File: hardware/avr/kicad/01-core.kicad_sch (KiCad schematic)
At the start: 18 parts, among them U1 ATmega1284P-PU, Y1 8MHz

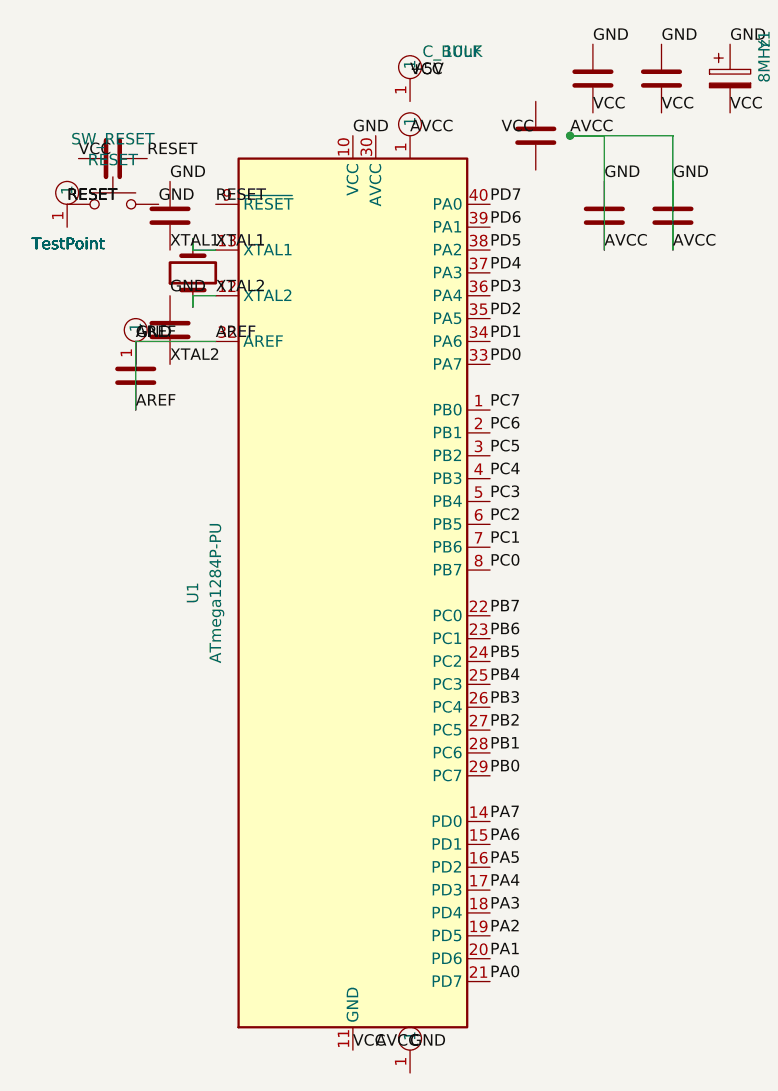
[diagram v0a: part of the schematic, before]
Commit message: Align AVR net labels with actual MCU pin endpoints
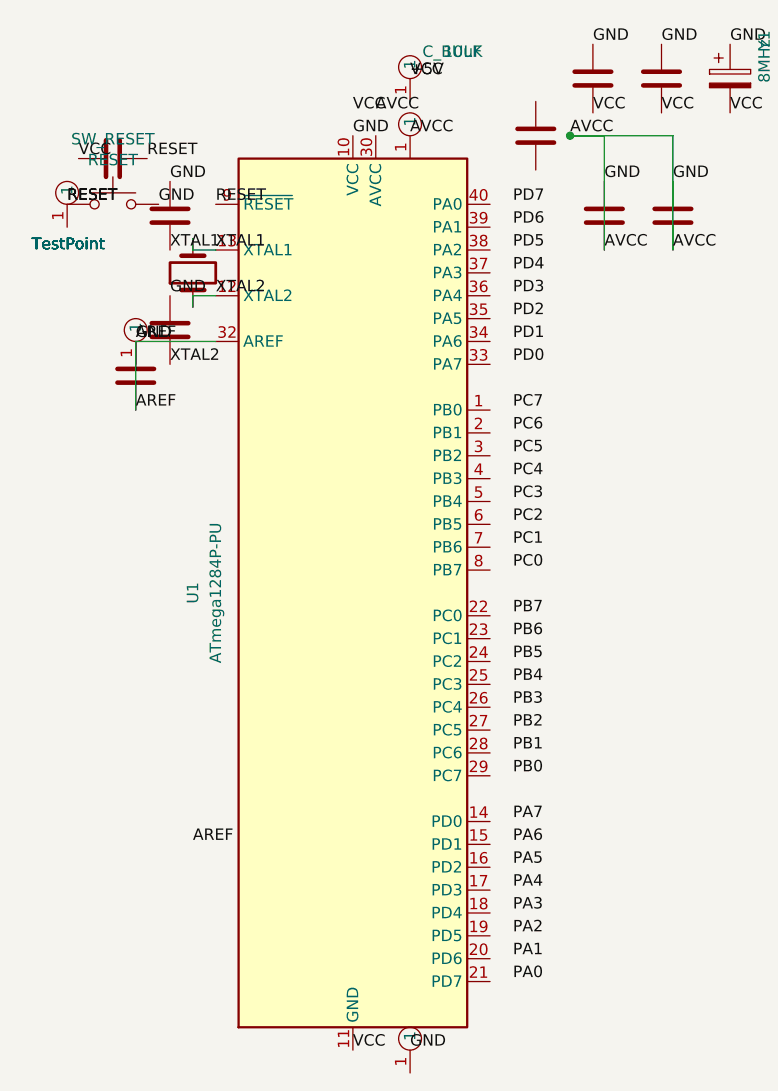
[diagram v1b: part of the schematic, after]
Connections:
- net PA0: no longer U1.21 (PD7)
- net PA1: no longer U1.20 (PD6)
- net PA2: no longer U1.19 (PD5)
- net PA3: no longer U1.18 (PD4)
- net PA4: no longer U1.17 (PD3)
- net PA5: no longer U1.16 (PD2)
- net PA6: no longer U1.15 (PD1)
- net PA7: no longer U1.14 (PD0)
- net PB0: no longer U1.29 (PC7)
- net PB1: no longer U1.28 (PC6)
- net PB2: no longer U1.27 (PC5)
- net PB3: no longer U1.26 (PC4)
- net PB4: no longer U1.25 (PC3)
- net PB5: no longer U1.24 (PC2)
- net PB6: no longer U1.23 (PC1)
- net PB7: no longer U1.22 (PC0)
- net PC0: no longer U1.8 (PB7)
- net PC1: no longer U1.7 (PB6)
- net PC2: no longer U1.6 (PB5)
- net PC3: no longer U1.5 (PB4)
- net PC4: no longer U1.4 (PB3)
- net PC5: no longer U1.3 (PB2)
- net PC6: no longer U1.2 (PB1)
- net PC7: no longer U1.1 (PB0)
- net PD0: no longer U1.33 (PA7)
- net PD1: no longer U1.34 (PA6)
- net PD2: no longer U1.35 (PA5)
- net PD3: no longer U1.36 (PA4)
- net PD4: no longer U1.37 (PA3)
- net PD5: no longer U1.38 (PA2)
- net PD6: no longer U1.39 (PA1)
- net PD7: no longer U1.40 (PA0)
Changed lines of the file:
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@@
 (kicad_sch (version 20230121) (generator eeschema)
   (paper "A4")
-  (label "PB0" (at 72.39 100.33 0) (fields_autoplaced)
+  (label "PB0" (at 74.93 100.33 0) (fields_autoplaced)
     (effects (font (size 1.27 1.27)) (justify left bottom))
   )
-  (label "PB1" (at 72.39 97.79 0) (fields_autoplaced)
+  (label "PB1" (at 74.93 97.79 0) (fields_autoplaced)
     (effects (font (size 1.27 1.27)) (justify left bottom))
   )
-  (label "PB2" (at 72.39 95.25 0) (fields_autoplaced)
+  (label "PB2" (at 74.93 95.25 0) (fields_autoplaced)
     (effects (font (size 1.27 1.27)) (justify left bottom))
   )
-  (label "PB3" (at 72.39 92.71 0) (fields_autoplaced)
+  (label "PB3" (at 74.93 92.71 0) (fields_autoplaced)
     (effects (font (size 1.27 1.27)) (justify left bottom))
   )
-  (label "PB4" (at 72.39 90.17 0) (fields_autoplaced)
+  (label "PB4" (at 74.93 90.17 0) (fields_autoplaced)
     (effects (font (size 1.27 1.27)) (justify left bottom))
   )
-  (label "PB5" (at 72.39 87.63 0) (fields_autoplaced)
+  (label "PB5" (at 74.93 87.63 0) (fields_autoplaced)
     (effects (font (size 1.27 1.27)) (justify left bottom))
   )
-  (label "PB6" (at 72.39 85.09 0) (fields_autoplaced)
+  (label "PB6" (at 74.93 85.09 0) (fields_autoplaced)
     (effects (font (size 1.27 1.27)) (justify left bottom))
   )
-  (label "PB7" (at 72.39 82.55 0) (fields_autoplaced)
+  (label "PB7" (at 74.93 82.55 0) (fields_autoplaced)
     (effects (font (size 1.27 1.27)) (justify left bottom))
   )
-  (label "PC0" (at 72.39 77.47 0) (fields_autoplaced)
+  (label "PC0" (at 74.93 77.47 0) (fields_autoplaced)
     (effects (font (size 1.27 1.27)) (justify left bottom))
   )
-  (label "PC1" (at 72.39 74.93 0) (fields_autoplaced)
+  (label "PC1" (at 74.93 74.93 0) (fields_autoplaced)
     (effects (font (size 1.27 1.27)) (justify left bottom))
   )
-  (label "PC2" (at 72.39 72.39 0) (fields_autoplaced)
+  (label "PC2" (at 74.93 72.39 0) (fields_autoplaced)
     (effects (font (size 1.27 1.27)) (justify left bottom))
   )
-  (label "PC3" (at 72.39 69.85 0) (fields_autoplaced)
+  (label "PC3" (at 74.93 69.85 0) (fields_autoplaced)
     (effects (font (size 1.27 1.27)) (justify left bottom))
   )
-  (label "PC4" (at 72.39 67.31 0) (fields_autoplaced)
+  (label "PC4" (at 74.93 67.31 0) (fields_autoplaced)
     (effects (font (size 1.27 1.27)) (justify left bottom))
   )
-  (label "PC5" (at 72.39 64.77 0) (fields_autoplaced)
+  (label "PC5" (at 74.93 64.77 0) (fields_autoplaced)
     (effects (font (size 1.27 1.27)) (justify left bottom))
   )
-  (label "PC6" (at 72.39 62.23 0) (fields_autoplaced)
+  (label "PC6" (at 74.93 62.23 0) (fields_autoplaced)
     (effects (font (size 1.27 1.27)) (justify left bottom))
   )
-  (label "PC7" (at 72.39 59.69 0) (fields_autoplaced)
+  (label "PC7" (at 74.93 59.69 0) (fields_autoplaced)
     (effects (font (size 1.27 1.27)) (justify left bottom))
   )
-  (label "PD0" (at 72.39 54.61 0) (fields_autoplaced)
+  (label "PD0" (at 74.93 54.61 0) (fields_autoplaced)
     (effects (font (size 1.27 1.27)) (justify left bottom))
   )
-  (label "PD1" (at 72.39 52.07 0) (fields_autoplaced)
+  (label "PD1" (at 74.93 52.07 0) (fields_autoplaced)
     (effects (font (size 1.27 1.27)) (justify left bottom))
   )
-  (label "PD2" (at 72.39 49.53 0) (fields_autoplaced)
+  (label "PD2" (at 74.93 49.53 0) (fields_autoplaced)
     (effects (font (size 1.27 1.27)) (justify left bottom))
   )
-  (label "PD3" (at 72.39 46.99 0) (fields_autoplaced)
+  (label "PD3" (at 74.93 46.99 0) (fields_autoplaced)
     (effects (font (size 1.27 1.27)) (justify left bottom))
   )
-  (label "PD4" (at 72.39 44.45 0) (fields_autoplaced)
+  (label "PD4" (at 74.93 44.45 0) (fields_autoplaced)
     (effects (font (size 1.27 1.27)) (justify left bottom))
   )
-  (label "PD5" (at 72.39 41.91 0) (fields_autoplaced)
+  (label "PD5" (at 74.93 41.91 0) (fields_autoplaced)
     (effects (font (size 1.27 1.27)) (justify left bottom))
   )
-  (label "PD6" (at 72.39 39.37 0) (fields_autoplaced)
+  (label "PD6" (at 74.93 39.37 0) (fields_autoplaced)
     (effects (font (size 1.27 1.27)) (justify left bottom))
   )
-  (label "PD7" (at 72.39 36.83 0) (fields_autoplaced)
+  (label "PD7" (at 74.93 36.83 0) (fields_autoplaced)
     (effects (font (size 1.27 1.27)) (justify left bottom))
   )
-  (label "PA7" (at 72.39 105.41 0) (fields_autoplaced)
+  (label "PA7" (at 74.93 105.41 0) (fields_autoplaced)
     (effects (font (size 1.27 1.27)) (justify left bottom))
   )
-  (label "PA6" (at 72.39 107.95 0) (fields_autoplaced)
+  (label "PA6" (at 74.93 107.95 0) (fields_autoplaced)
     (effects (font (size 1.27 1.27)) (justify left bottom))
   )
-  (label "PA5" (at 72.39 110.49 0) (fields_autoplaced)
+  (label "PA5" (at 74.93 110.49 0) (fields_autoplaced)
     (effects (font (size 1.27 1.27)) (justify left bottom))
   )
-  (label "PA4" (at 72.39 113.03 0) (fields_autoplaced)
+  (label "PA4" (at 74.93 113.03 0) (fields_autoplaced)
     (effects (font (size 1.27 1.27)) (justify left bottom))
   )
-  (label "PA3" (at 72.39 115.57 0) (fields_autoplaced)
+  (label "PA3" (at 74.93 115.57 0) (fields_autoplaced)
     (effects (font (size 1.27 1.27)) (justify left bottom))
   )
-  (label "PA2" (at 72.39 118.11 0) (fields_autoplaced)
+  (label "PA2" (at 74.93 118.11 0) (fields_autoplaced)
     (effects (font (size 1.27 1.27)) (justify left bottom))
   )
-  (label "PA1" (at 72.39 120.65 0) (fields_autoplaced)
+  (label "PA1" (at 74.93 120.65 0) (fields_autoplaced)
     (effects (font (size 1.27 1.27)) (justify left bottom))
   )
-  (label "PA0" (at 72.39 123.19 0) (fields_autoplaced)
+  (label "PA0" (at 74.93 123.19 0) (fields_autoplaced)
     (effects (font (size 1.27 1.27)) (justify left bottom))
   )
@@
     (effects (font (size 1.27 1.27)) (justify left bottom))
   )
-  (label "AVCC" (at 59.69 130.81 0) (fields_autoplaced)
+  (label "AVCC" (at 59.69 26.67 0) (fields_autoplaced)
     (effects (font (size 1.27 1.27)) (justify left bottom))
   )
-  (label "AREF" (at 41.91 52.07 0) (fields_autoplaced)
+  (label "AREF" (at 39.37 107.95 0) (fields_autoplaced)
     (effects (font (size 1.27 1.27)) (justify left bottom))
   )
@@
     (effects (font (size 1.27 1.27)) (justify left bottom))
   )
-  (label "VCC" (at 73.66 29.21 0) (fields_autoplaced)
+  (label "VCC" (at 57.15 26.67 0) (fields_autoplaced)
     (effects (font (size 1.27 1.27)) (justify left bottom))
   )

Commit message: Map AVR labels to KiCad-reported pin coordinates
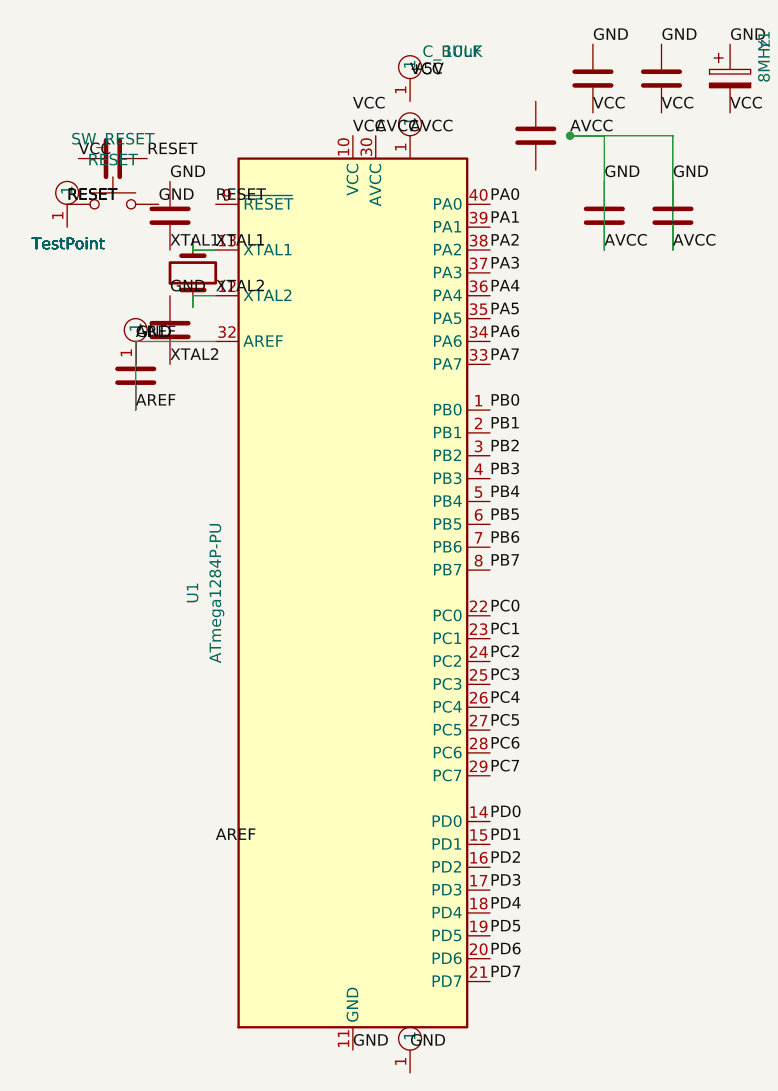
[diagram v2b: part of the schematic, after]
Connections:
- net +5V: now also U1.10 (VCC); no longer U1.11 (GND), U1.31 (GND)
- net AREF: now also U1.11 (GND), U1.30 (AVCC), U1.31 (GND); no longer U1.10 (VCC)
- net PA0: now also U1.40 (PA0)
- net PA1: now also U1.39 (PA1)
- net PA2: now also U1.38 (PA2)
- net PA3: now also U1.37 (PA3)
- net PA4: now also U1.36 (PA4)
- net PA5: now also U1.35 (PA5)
- net PA6: now also U1.34 (PA6)
- net PA7: now also U1.33 (PA7)
- net PB0: now also U1.1 (PB0)
- net PB1: now also U1.2 (PB1)
- net PB2: now also U1.3 (PB2)
- net PB3: now also U1.4 (PB3)
- net PB4: now also U1.5 (PB4)
- net PB5: now also U1.6 (PB5)
- net PB6: now also U1.7 (PB6)
- net PB7: now also U1.8 (PB7)
- net PC0: now also U1.22 (PC0)
- net PC1: now also U1.23 (PC1)
- net PC2: now also U1.24 (PC2)
- net PC3: now also U1.25 (PC3)
- net PC4: now also U1.26 (PC4)
- net PC5: now also U1.27 (PC5)
- net PC6: now also U1.28 (PC6)
- net PC7: now also U1.29 (PC7)
- net PD0: now also U1.14 (PD0)
- net PD1: now also U1.15 (PD1)
- net PD2: now also U1.16 (PD2)
- net PD3: now also U1.17 (PD3)
- net PD4: now also U1.18 (PD4)
- net PD5: now also U1.19 (PD5)
- net PD6: now also U1.20 (PD6)
- net PD7: now also U1.21 (PD7)
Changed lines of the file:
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@@
 (kicad_sch (version 20230121) (generator eeschema)
   (paper "A4")
-  (label "PB0" (at 74.93 100.33 0) (fields_autoplaced)
+  (label "PB0" (at 72.39 59.69 0) (fields_autoplaced)
     (effects (font (size 1.27 1.27)) (justify left bottom))
   )
-  (label "PB1" (at 74.93 97.79 0) (fields_autoplaced)
+  (label "PB1" (at 72.39 62.23 0) (fields_autoplaced)
     (effects (font (size 1.27 1.27)) (justify left bottom))
   )
-  (label "PB2" (at 74.93 95.25 0) (fields_autoplaced)
+  (label "PB2" (at 72.39 64.77 0) (fields_autoplaced)
     (effects (font (size 1.27 1.27)) (justify left bottom))
   )
-  (label "PB3" (at 74.93 92.71 0) (fields_autoplaced)
+  (label "PB3" (at 72.39 67.31 0) (fields_autoplaced)
     (effects (font (size 1.27 1.27)) (justify left bottom))
   )
-  (label "PB4" (at 74.93 90.17 0) (fields_autoplaced)
+  (label "PB4" (at 72.39 69.85 0) (fields_autoplaced)
     (effects (font (size 1.27 1.27)) (justify left bottom))
   )
-  (label "PB5" (at 74.93 87.63 0) (fields_autoplaced)
+  (label "PB5" (at 72.39 72.39 0) (fields_autoplaced)
     (effects (font (size 1.27 1.27)) (justify left bottom))
   )
-  (label "PB6" (at 74.93 85.09 0) (fields_autoplaced)
+  (label "PB6" (at 72.39 74.93 0) (fields_autoplaced)
     (effects (font (size 1.27 1.27)) (justify left bottom))
   )
-  (label "PB7" (at 74.93 82.55 0) (fields_autoplaced)
+  (label "PB7" (at 72.39 77.47 0) (fields_autoplaced)
     (effects (font (size 1.27 1.27)) (justify left bottom))
   )
-  (label "PC0" (at 74.93 77.47 0) (fields_autoplaced)
+  (label "PC0" (at 72.39 82.55 0) (fields_autoplaced)
     (effects (font (size 1.27 1.27)) (justify left bottom))
   )
-  (label "PC1" (at 74.93 74.93 0) (fields_autoplaced)
+  (label "PC1" (at 72.39 85.09 0) (fields_autoplaced)
     (effects (font (size 1.27 1.27)) (justify left bottom))
   )
-  (label "PC2" (at 74.93 72.39 0) (fields_autoplaced)
+  (label "PC2" (at 72.39 87.63 0) (fields_autoplaced)
     (effects (font (size 1.27 1.27)) (justify left bottom))
   )
-  (label "PC3" (at 74.93 69.85 0) (fields_autoplaced)
+  (label "PC3" (at 72.39 90.17 0) (fields_autoplaced)
     (effects (font (size 1.27 1.27)) (justify left bottom))
   )
-  (label "PC4" (at 74.93 67.31 0) (fields_autoplaced)
+  (label "PC4" (at 72.39 92.71 0) (fields_autoplaced)
     (effects (font (size 1.27 1.27)) (justify left bottom))
   )
-  (label "PC5" (at 74.93 64.77 0) (fields_autoplaced)
+  (label "PC5" (at 72.39 95.25 0) (fields_autoplaced)
     (effects (font (size 1.27 1.27)) (justify left bottom))
   )
-  (label "PC6" (at 74.93 62.23 0) (fields_autoplaced)
+  (label "PC6" (at 72.39 97.79 0) (fields_autoplaced)
     (effects (font (size 1.27 1.27)) (justify left bottom))
   )
-  (label "PC7" (at 74.93 59.69 0) (fields_autoplaced)
+  (label "PC7" (at 72.39 100.33 0) (fields_autoplaced)
     (effects (font (size 1.27 1.27)) (justify left bottom))
   )
-  (label "PD0" (at 74.93 54.61 0) (fields_autoplaced)
+  (label "PD0" (at 72.39 105.41 0) (fields_autoplaced)
     (effects (font (size 1.27 1.27)) (justify left bottom))
   )
-  (label "PD1" (at 74.93 52.07 0) (fields_autoplaced)
+  (label "PD1" (at 72.39 107.95 0) (fields_autoplaced)
     (effects (font (size 1.27 1.27)) (justify left bottom))
   )
-  (label "PD2" (at 74.93 49.53 0) (fields_autoplaced)
+  (label "PD2" (at 72.39 110.49 0) (fields_autoplaced)
     (effects (font (size 1.27 1.27)) (justify left bottom))
   )
-  (label "PD3" (at 74.93 46.99 0) (fields_autoplaced)
+  (label "PD3" (at 72.39 113.03 0) (fields_autoplaced)
     (effects (font (size 1.27 1.27)) (justify left bottom))
   )
-  (label "PD4" (at 74.93 44.45 0) (fields_autoplaced)
+  (label "PD4" (at 72.39 115.57 0) (fields_autoplaced)
     (effects (font (size 1.27 1.27)) (justify left bottom))
   )
-  (label "PD5" (at 74.93 41.91 0) (fields_autoplaced)
+  (label "PD5" (at 72.39 118.11 0) (fields_autoplaced)
     (effects (font (size 1.27 1.27)) (justify left bottom))
   )
-  (label "PD6" (at 74.93 39.37 0) (fields_autoplaced)
+  (label "PD6" (at 72.39 120.65 0) (fields_autoplaced)
     (effects (font (size 1.27 1.27)) (justify left bottom))
   )
-  (label "PD7" (at 74.93 36.83 0) (fields_autoplaced)
+  (label "PD7" (at 72.39 123.19 0) (fields_autoplaced)
     (effects (font (size 1.27 1.27)) (justify left bottom))
   )
-  (label "PA7" (at 74.93 105.41 0) (fields_autoplaced)
+  (label "PA7" (at 72.39 54.61 0) (fields_autoplaced)
     (effects (font (size 1.27 1.27)) (justify left bottom))
   )
-  (label "PA6" (at 74.93 107.95 0) (fields_autoplaced)
+  (label "PA6" (at 72.39 52.07 0) (fields_autoplaced)
     (effects (font (size 1.27 1.27)) (justify left bottom))
   )
-  (label "PA5" (at 74.93 110.49 0) (fields_autoplaced)
+  (label "PA5" (at 72.39 49.53 0) (fields_autoplaced)
     (effects (font (size 1.27 1.27)) (justify left bottom))
   )
-  (label "PA4" (at 74.93 113.03 0) (fields_autoplaced)
+  (label "PA4" (at 72.39 46.99 0) (fields_autoplaced)
     (effects (font (size 1.27 1.27)) (justify left bottom))
   )
-  (label "PA3" (at 74.93 115.57 0) (fields_autoplaced)
+  (label "PA3" (at 72.39 44.45 0) (fields_autoplaced)
     (effects (font (size 1.27 1.27)) (justify left bottom))
   )
-  (label "PA2" (at 74.93 118.11 0) (fields_autoplaced)
+  (label "PA2" (at 72.39 41.91 0) (fields_autoplaced)
     (effects (font (size 1.27 1.27)) (justify left bottom))
   )
-  (label "PA1" (at 74.93 120.65 0) (fields_autoplaced)
+  (label "PA1" (at 72.39 39.37 0) (fields_autoplaced)
     (effects (font (size 1.27 1.27)) (justify left bottom))
   )
-  (label "PA0" (at 74.93 123.19 0) (fields_autoplaced)
+  (label "PA0" (at 72.39 36.83 0) (fields_autoplaced)
     (effects (font (size 1.27 1.27)) (justify left bottom))
   )
-  (label "VCC" (at 57.15 130.81 0) (fields_autoplaced)
+  (label "VCC" (at 57.15 29.21 0) (fields_autoplaced)
     (effects (font (size 1.27 1.27)) (justify left bottom))
   )
-  (label "GND" (at 57.15 29.21 0) (fields_autoplaced)
+  (label "GND" (at 57.15 130.81 0) (fields_autoplaced)
     (effects (font (size 1.27 1.27)) (justify left bottom))
   )
-  (label "AVCC" (at 59.69 26.67 0) (fields_autoplaced)
+  (label "AVCC" (at 59.69 29.21 0) (fields_autoplaced)
     (effects (font (size 1.27 1.27)) (justify left bottom))
   )
-  (label "AREF" (at 39.37 107.95 0) (fields_autoplaced)
+  (label "AREF" (at 41.91 107.95 0) (fields_autoplaced)
     (effects (font (size 1.27 1.27)) (justify left bottom))
   )
